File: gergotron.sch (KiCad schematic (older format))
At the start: 14 parts, among them J1 KMDGX-6S-BS, J2 KMDGX-6S-BS, P1 Power, P2 Analog, P3 Digital, P4 Digital, P5 CONN_01X01, P6 CONN_01X01, P7 CONN_01X01, P8 CONN_01X01, U1 TXB0104D

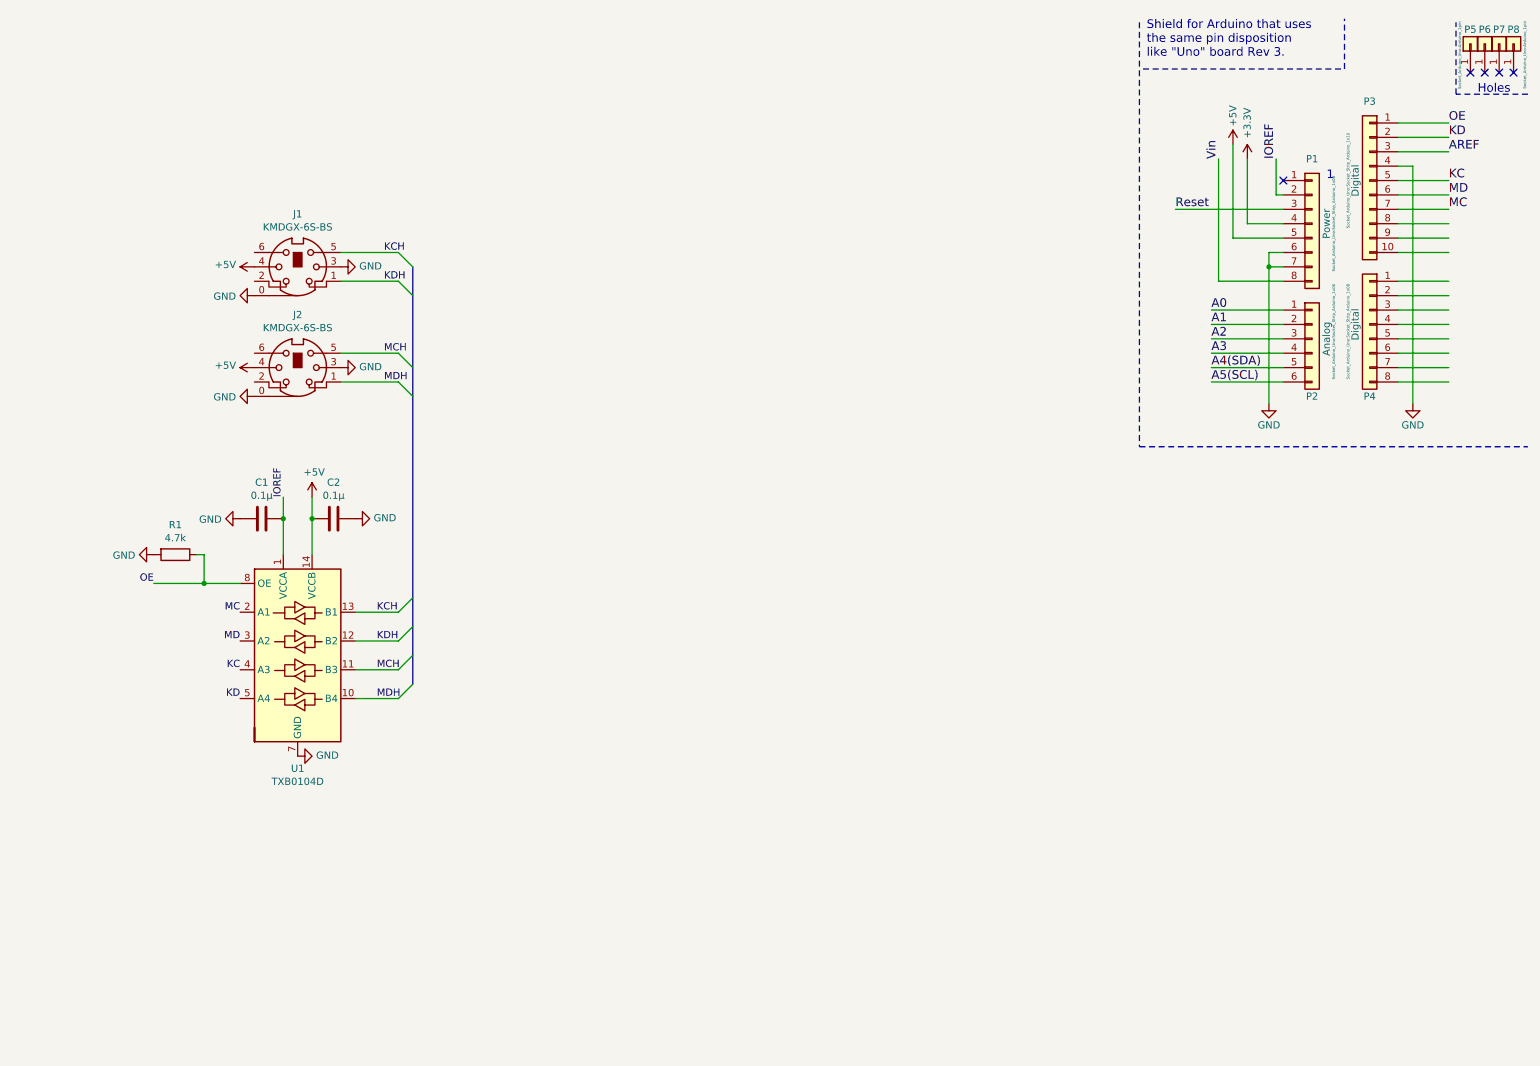
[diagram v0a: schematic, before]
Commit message: Add audio in
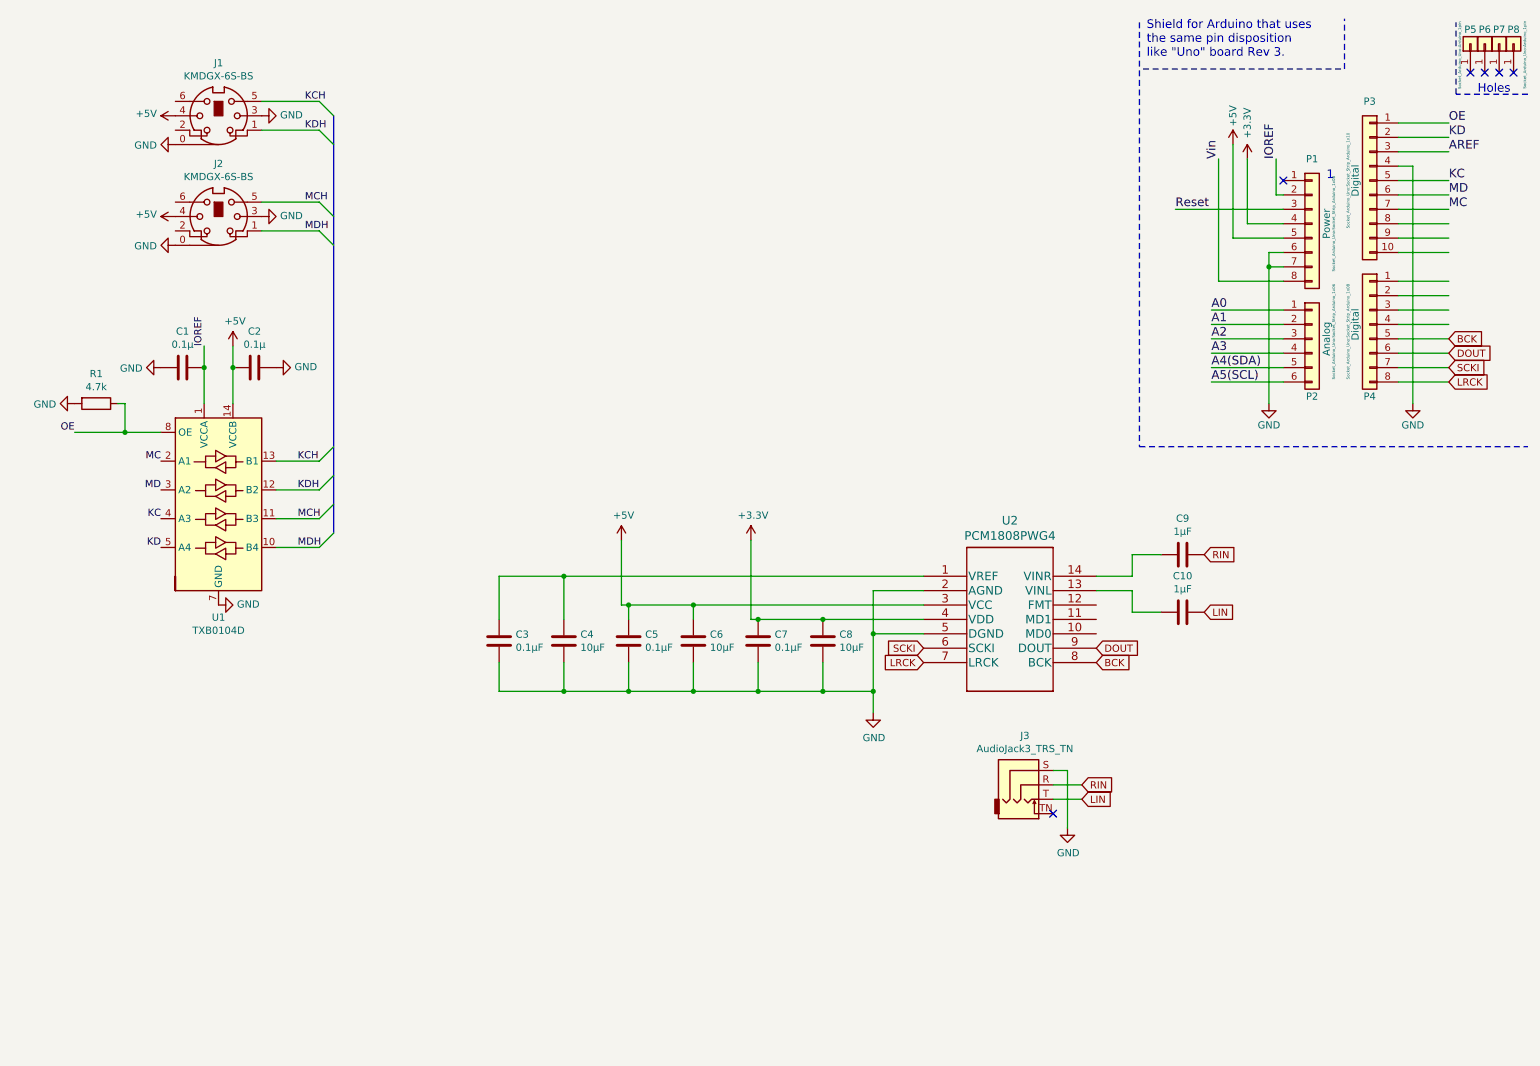
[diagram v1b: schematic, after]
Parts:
- added C10, C9: 1μF, Capacitor_SMD:C_0603_1608Metric, symbol Device:C
- added C3, C5, C7: 0.1μF, Capacitor_SMD:C_0603_1608Metric, symbol Device:C
- added C4, C6, C8: 10μF, Capacitor_SMD:C_0805_2012Metric, symbol Device:C
- added J3: AudioJack3_TRS_TN, gergotron:sj-352x-smt, symbol audioJack3_TRS_TN:AudioJack3_TRS_TN
- added U2: PCM1808PWG4, pcm1808:PCM1808PWG4, symbol pcm1808:PCM1808PWG4
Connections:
- net labels added: BCK, DOUT, LIN, LRCK, RIN, SCKI
- wire segments 54 -> 95
- no-connect marks 5 -> 6
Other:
- moved on the sheet: C1, C2, J1, J2, R1, U1

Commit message: Add oled display
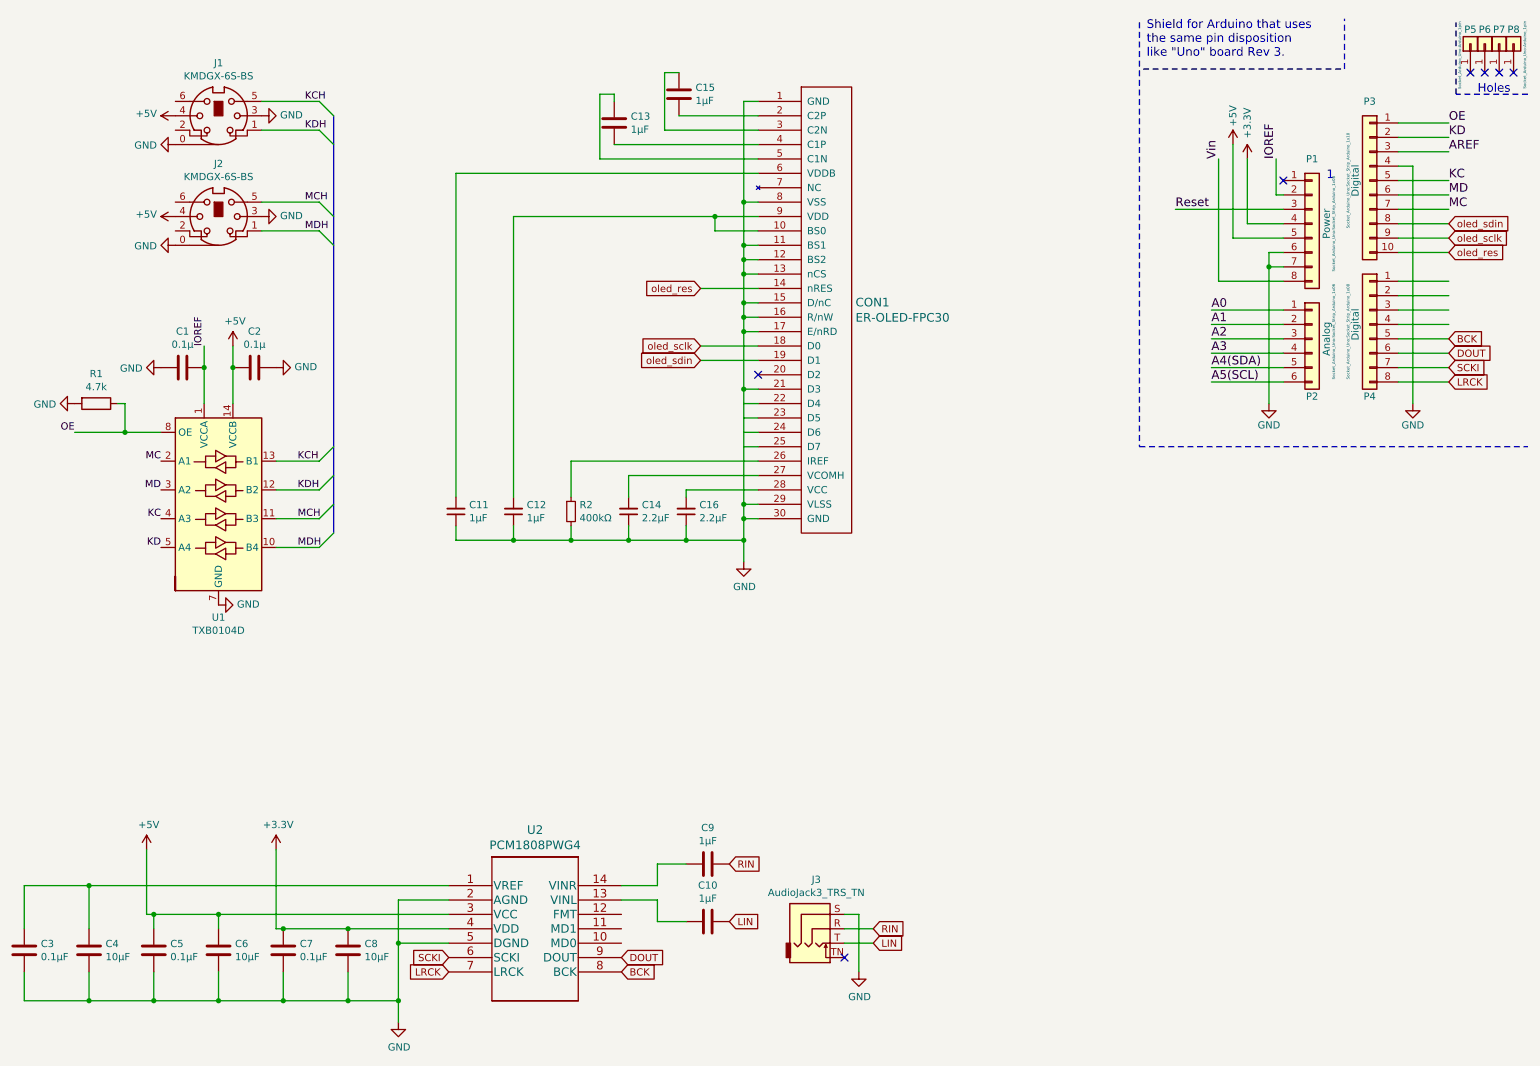
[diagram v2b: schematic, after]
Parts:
- added C11, C12: 1μF, Capacitor_SMD:C_0603_1608Metric, symbol Device:C_Small
- added C13, C15: 1μF, Capacitor_SMD:C_0603_1608Metric, symbol Device:C
- added C14, C16: 2.2μF, Capacitor_SMD:C_0603_1608Metric, symbol Device:C_Small
- added CON1: ER-OLED-FPC30, gergotron:er-oled-fpc30-flipped, symbol er-oled-fpc30:ER-OLED-FPC30
- added R2: 400kΩ, Resistor_SMD:R_0603_1608Metric, symbol Device:R_Small
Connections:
- net labels added: oled_res, oled_sclk, oled_sdin
- wire segments 95 -> 157
- no-connect marks 6 -> 7
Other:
- moved on the sheet: C10, C3, C4, C5, C6, C7, C8, C9, J3, U2

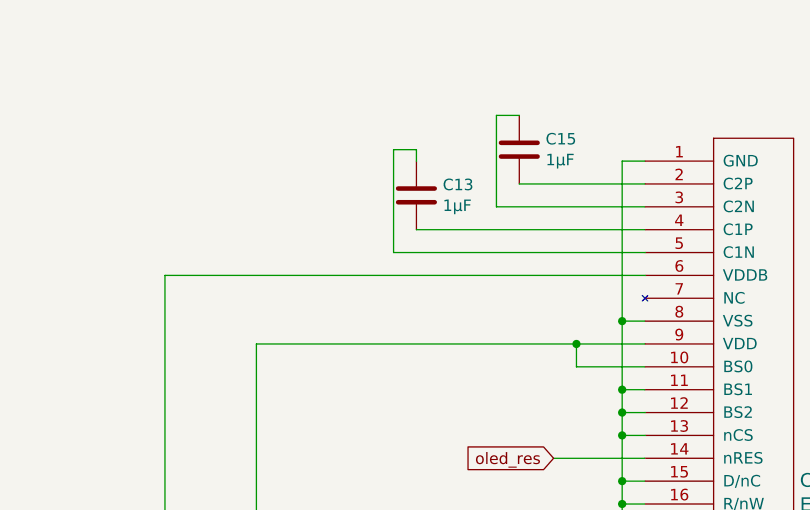
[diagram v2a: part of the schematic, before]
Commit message: power to the oled
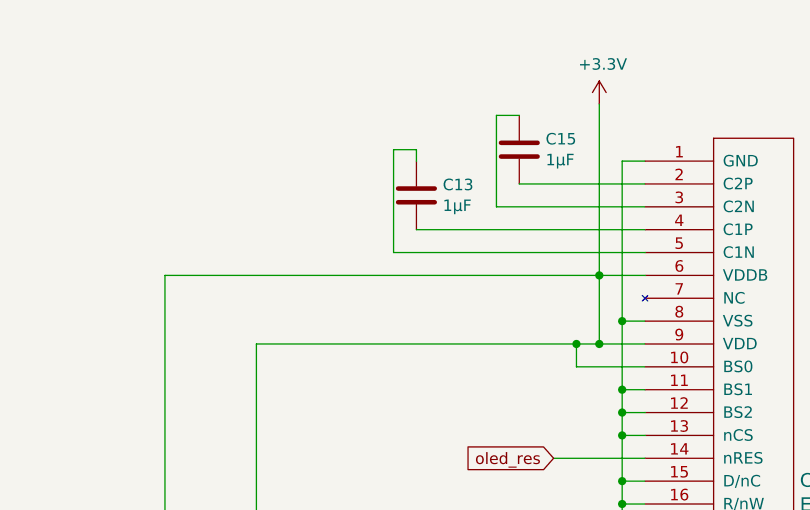
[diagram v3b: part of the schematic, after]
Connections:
- wire segments 157 -> 161
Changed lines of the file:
@@
 	4150 1850 5550 1850
 Wire Wire Line
-	5850 1550 3750 1550
+	5850 1550 5650 1550
 Wire Wire Line
 	3750 1550 3750 3800
@@
 Connection ~ 5550 1850
 Wire Wire Line
-	5550 1850 5850 1850
+	5550 1850 5650 1850
 Wire Wire Line
 	5850 2050 5750 2050
@@
 Wire Wire Line
 	5750 2250 5750 2450
+Wire Wire Line
+	5650 1850 5650 1550
+Connection ~ 5650 1850
+Wire Wire Line
+	5650 1850 5850 1850
+Connection ~ 5650 1550
+Wire Wire Line
+	5650 1550 3750 1550
+Wire Wire Line
+	5650 1550 5650 800
 Wire Bus Line
 	2900 1150 2900 4050
+$Comp
+L power:+3.3V #PWR0121
+U 1 1 5C151946
+P 5650 800
+F 0 "#PWR0121" H 5650 650 50  0001 C CNN
+F 1 "+3.3V" H 5665 973 50  0000 C CNN
+F 2 "" H 5650 800 50  0001 C CNN
+F 3 "" H 5650 800 50  0001 C CNN
+	1    5650 800
+	1    0    0    -1
+$EndComp
 $EndSCHEMATC

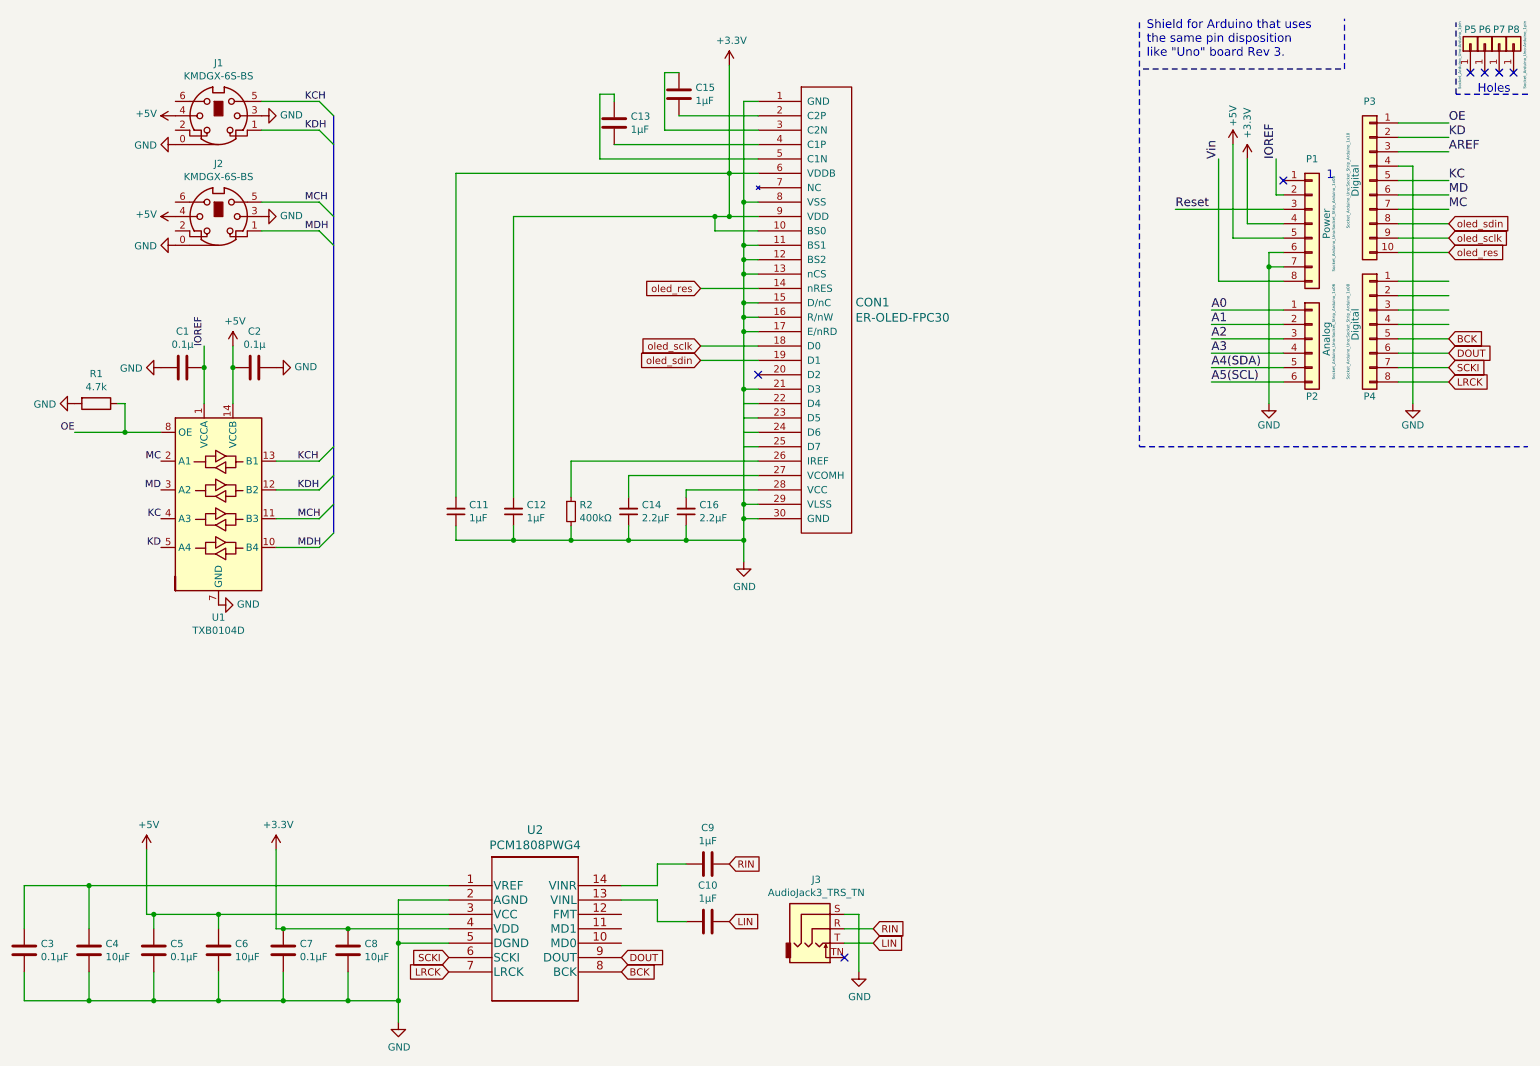
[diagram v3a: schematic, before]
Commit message: Tidy up schematic and connect unused data wires to gnd
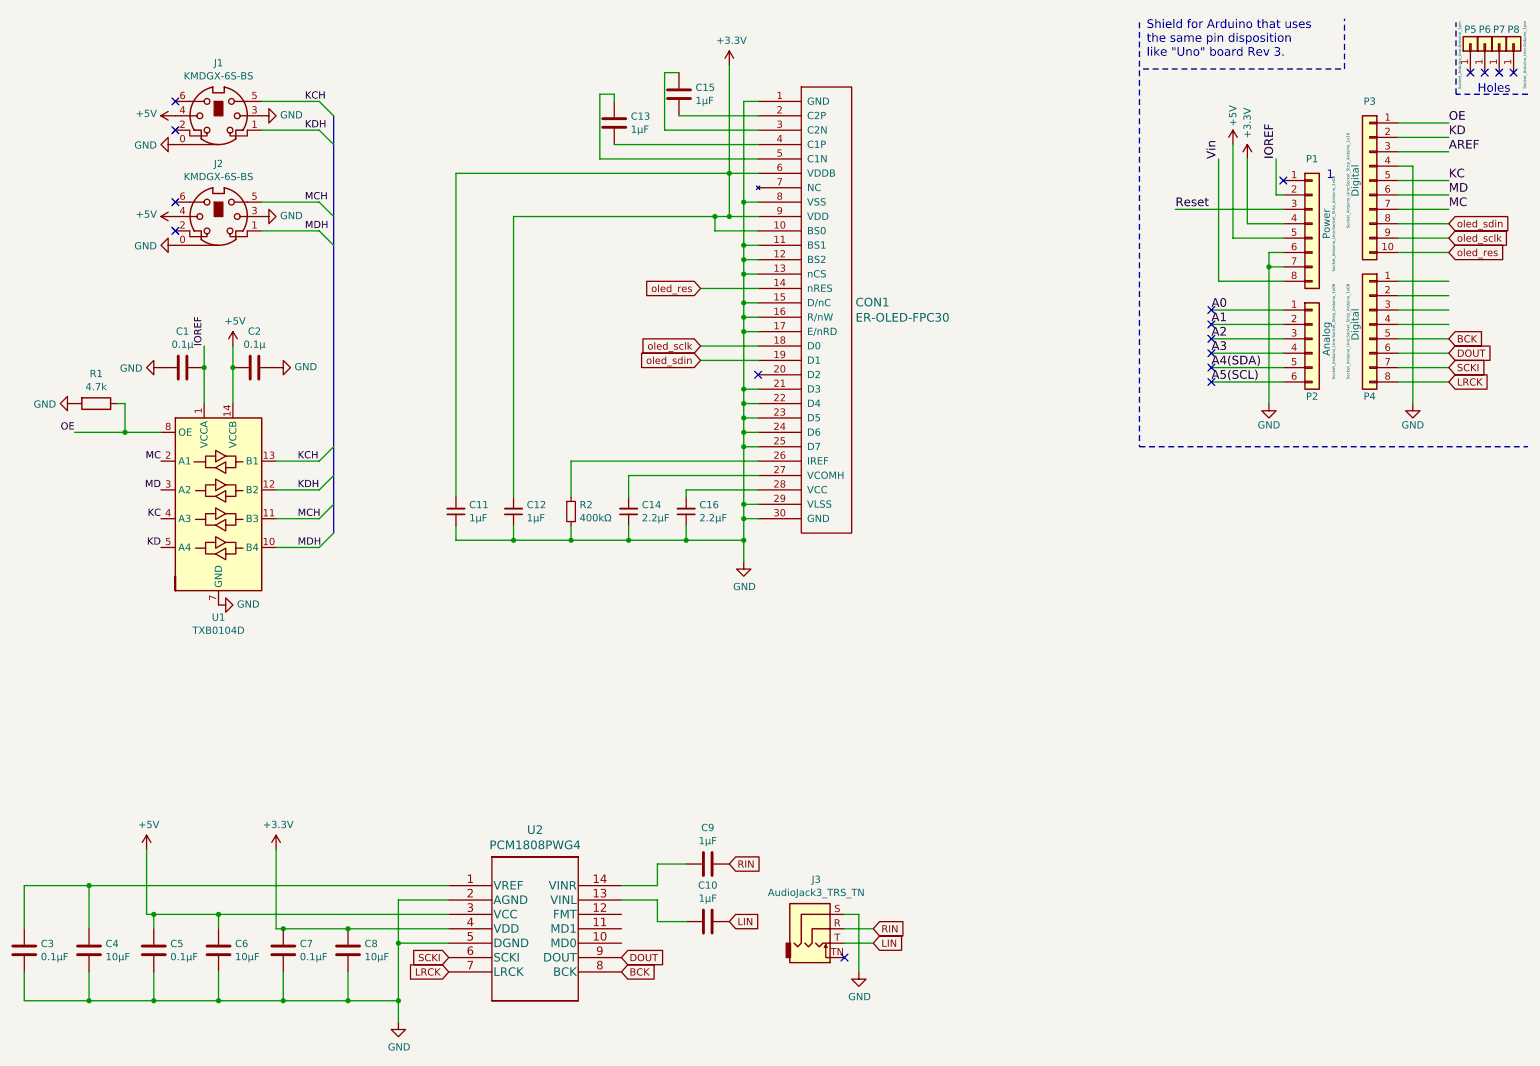
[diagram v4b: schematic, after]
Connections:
- wire segments 161 -> 165
- no-connect marks 7 -> 17
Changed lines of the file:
@@
 EESchema Schematic File Version 4
 LIBS:gergotron-cache
-LIBS:ergotron-cache
 EELAYER 26 0
 EELAYER END
@@
 Connection ~ 5750 3050
 Wire Wire Line
-	5750 3050 5750 3850
+	5750 3050 5750 3150
 Wire Wire Line
 	5850 3150 5750 3150
@@
 Wire Wire Line
 	5650 1550 5650 800
-Wire Bus Line
-	2900 1150 2900 4050
 $Comp
 L power:+3.3V #PWR0121
@@
 	1    0    0    -1
 $EndComp
+Connection ~ 5750 3150
+Wire Wire Line
+	5750 3150 5750 3250
+Connection ~ 5750 3250
+Wire Wire Line
+	5750 3250 5750 3350
+Connection ~ 5750 3350
+Wire Wire Line
+	5750 3350 5750 3450
+Connection ~ 5750 3450
+Wire Wire Line
+	5750 3450 5750 3850
+NoConn ~ 1800 1050
+NoConn ~ 1800 1250
+NoConn ~ 1800 1750
+NoConn ~ 1800 1950
+NoConn ~ 9000 2500
+NoConn ~ 9000 2600
+NoConn ~ 9000 2700
+NoConn ~ 9000 2800
+NoConn ~ 9000 2900
+NoConn ~ 9000 3000
+Wire Bus Line
+	2900 1150 2900 4050
 $EndSCHEMATC
